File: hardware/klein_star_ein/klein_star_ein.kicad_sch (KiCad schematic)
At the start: 195 parts, among them J1 USB_A, J10 AudioJack3_Ground_Switch, J11 AudioJack3_Ground_Switch, J12 AudioJack3_Ground_Switch, J2 DB15_Female_HighDensity_Mount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, J3 Bus_PCI_Express_x1, J4 1367073-1, J5 ARJM11C7-502-AB-ER2-T, J6 USB_C_Receptacle, J7 MEM2051-00-195-00-A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

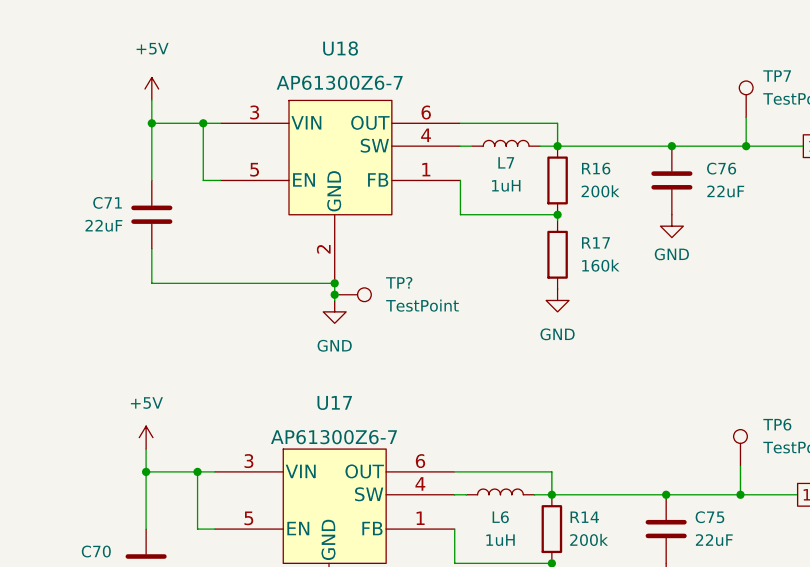
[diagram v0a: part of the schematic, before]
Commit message: Switched decupling caps to bigger size
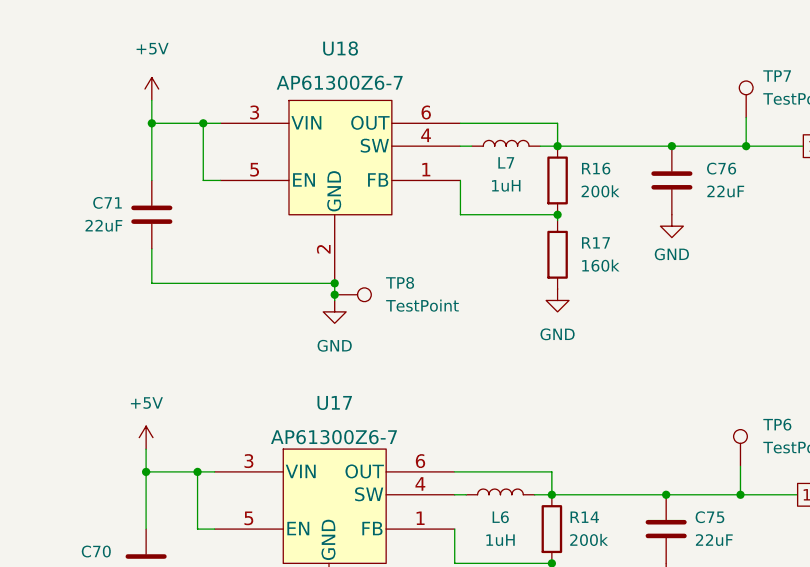
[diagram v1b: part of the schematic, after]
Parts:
- C77, C78, C79, C80, C81, C82, C83, C84, C85, C86, C87, C88, C89, C90, C92, C93, C94, C95: footprint Capacitor_SMD:C_0402_1005Metric -> Capacitor_SMD:C_0603_1608Metric
- gave numbers to parts that had none: 1
